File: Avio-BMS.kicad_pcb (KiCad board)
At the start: 2 copper layers, 80 x 80 mm, 102 parts, among them J1 MainBattery, J2 5077CR-16SMC2-BK-TR, J3 SubBattery, J4 Conn_01x03_Pin, J5 Conn_01x03_Pin, J6 +3.3V, J7 +6V, J8 +3.3V, J9 +6V, Q1 Si2333DDS-T1-GE3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

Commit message: update pcb
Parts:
- added C37: 0.1u, Capacitor_SMD:C_0603_1608Metric_Pad1.08x0.95mm_HandSolder, F.Cu at (157.2, 73.9)
- added C38: 1u, Capacitor_SMD:C_0603_1608Metric_Pad1.08x0.95mm_HandSolder, F.Cu at (160.4, 68.6)
- added C39: 43p, Capacitor_SMD:C_0603_1608Metric_Pad1.08x0.95mm_HandSolder, F.Cu at (165.7, 70.5)
- added C40: 1n, Capacitor_SMD:C_0603_1608Metric_Pad1.08x0.95mm_HandSolder, F.Cu at (167.3, 67.2)
- added R30: 28.7k, Resistor_SMD:R_0603_1608Metric_Pad0.98x0.95mm_HandSolder, F.Cu at (167.3, 70.5)
- C27: value C -> 8.2n
- R26: value R -> 115k
- moved C20 2.17 mm to (153.8, 77.7)
- moved C22 2.17 mm to (151.8, 77.7)
- moved C27 1.72 mm to (160.4, 79.4)
- moved R26 1.56 mm to (164.2, 68.6)
- moved C24 1.31 mm to (158.8, 77.4)
- moved D3 1.14 mm to (168.2, 119.0)
- moved R14 1.14 mm to (167.0, 117.7)
- moved R28 1.14 mm to (169.2, 70.8)
- moved R27 1.12 mm to (171.6, 71.7)
- moved R25 0.31 mm to (158.7, 72.0)
- moved C29 0.30 mm to (174.2, 74.4)
- moved C31 0.30 mm to (172.2, 74.4)
- moved C33 0.30 mm to (168.2, 74.4)
- moved C35 0.30 mm to (170.2, 74.4)
- moved C28 0.25 mm to (166.0, 74.4)
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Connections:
- net FB_{TPS61088} renamed /DCDC3.3V&7.4VOutput/FB_{TPS61088}
- U3 pad 16: (no net) -> GND
- U3 pad 17: (no net) -> GND
- U3 pad 18: (no net) -> GND
- U3 pad 19: (no net) -> GND
- U3 pad 20: (no net) -> GND
- U3 pad 21: (no net) -> GND
- U3 pad 22: (no net) -> GND
- U3 pad 23: (no net) -> GND
- U3 pad 24: (no net) -> GND
- U3 pad 25: (no net) -> GND
- U3 pad 26: (no net) -> GND
- U3 pad 27: (no net) -> GND
- U3 pad 28: (no net) -> GND
- U3 pad 29: (no net) -> GND
- U3 pad 30: (no net) -> GND
- U4 pad 1: unconnected-(U4-VCC_{TPS61088}-Pad1) -> /DCDC3.3V&7.4VOutput/EN_{TPS61088}
- U4 pad 13: unconnected-(U4-MODE-Pad13) -> GND
- U4 pad 18: unconnected-(U4-COMP-Pad18) -> /DCDC3.3V&7.4VOutput/COMP_{TPS61088}
- U4 pad 2: EN_{TPS61088} -> /DCDC3.3V&7.4VOutput/EN_{TPS61088}
- U4 pad 8: unconnected-(U4-BOOT-Pad8) -> Net-(U4-BOOT)
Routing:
- net +3.3V: track 71.3 -> 86.9 mm
- net +6V: track 100.0 -> 89.7 mm
- net VCC: track 91.0 -> 99.2 mm, vias 0 -> 2
- net /DCDC3.3V&7.4VOutput/COMP_{TPS61088}: track 0.00 -> 3.80 mm
- net NTC2: track 42.7 -> 39.2 mm
- net Net-(U4-BOOT): track 0.00 -> 3.38 mm
- net /DCDC3.3V&7.4VOutput/EN_{TPS61088}: track 0.00 -> 3.03 mm
- net NTC1: track 28.2 -> 25.7 mm
- net Net-(U4-SS): track 1.94 -> 3.61 mm
- net Net-(C40-Pad2): track 0.00 -> 1.53 mm
- net /DCDC3.3V&7.4VOutput/FB_{TPS61088}: track 6.20 -> 7.28 mm
- net GND: vias 10 -> 125
- added copper zone on F.Cu, net +6V
- added copper zone on B.Cu, net GND
- added copper zone on F.Cu, net GND
- added copper zone on F.Cu, net VCC

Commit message: update
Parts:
- moved D4 56.2 mm to (188.1, 104.5), turned to -90 degrees
- moved REF** 55.4 mm to (182.8, 111.2), turned to -45 degrees
- moved REF** 55.0 mm to (182.8, 60.3), turned to -45 degrees
- moved R23 54.3 mm to (186.5, 104.5), turned to 90 degrees
- moved D5 53.9 mm to (188.3, 100.5), turned to -90 degrees
- moved J3 52.5 mm to (189.3, 93.8), turned to 90 degrees
- moved D2 52.2 mm to (164.7, 50.5), turned to 0 degrees
- moved D3 51.9 mm to (186.6, 70.5), turned to 135 degrees
- moved R24 51.7 mm to (186.5, 100.6), turned to 90 degrees
- moved J1 51.3 mm to (189.3, 82.8), turned to 90 degrees
- moved TP1 50.1 mm to (175.0, 57.6), turned to -90 degrees
- moved R4 49.9 mm to (167.0, 53.1), turned to -90 degrees
- moved R14 49.5 mm to (185.4, 71.8), turned to 135 degrees
- moved REF** 47.2 mm to (131.9, 111.2), turned to -45 degrees
- moved J8 46.7 mm to (160.3, 117.8), turned to 0 degrees
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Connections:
- J5 pad 2: /Li-ionBatteryCharger,PowerPath/D1 -> /Li-ionBatteryCharger,PowerPath/D2
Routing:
- net /Li-ionBatteryCharger,PowerPath/D2: track 0.00 -> 16.3 mm, vias 0 -> 1
- net (no net): track 16.3 -> 0.00 mm, vias 1 -> 0
- net Net-(U3-EN): track 2.13 -> 17.3 mm, vias 0 -> 2
- net V1: track 94.6 -> 87.8 mm, vias 27 -> 33
- net VCC: track 99.2 -> 97.2 mm
- net Net-(Q3B-S2): track 35.1 -> 35.7 mm
- net GND: vias 125 -> 449

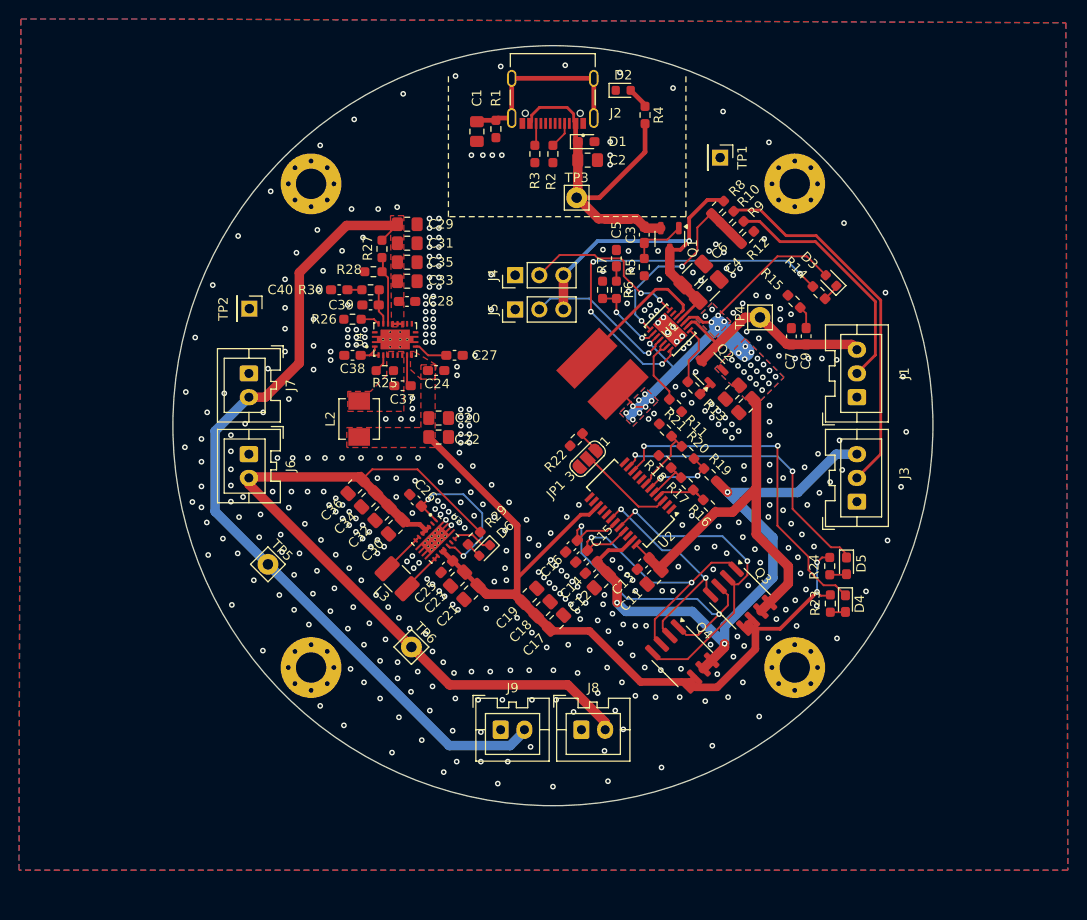
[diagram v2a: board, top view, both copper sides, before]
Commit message: remove autosave and lock files; update component values and footprints; add new drill and Gerber files; create BOM
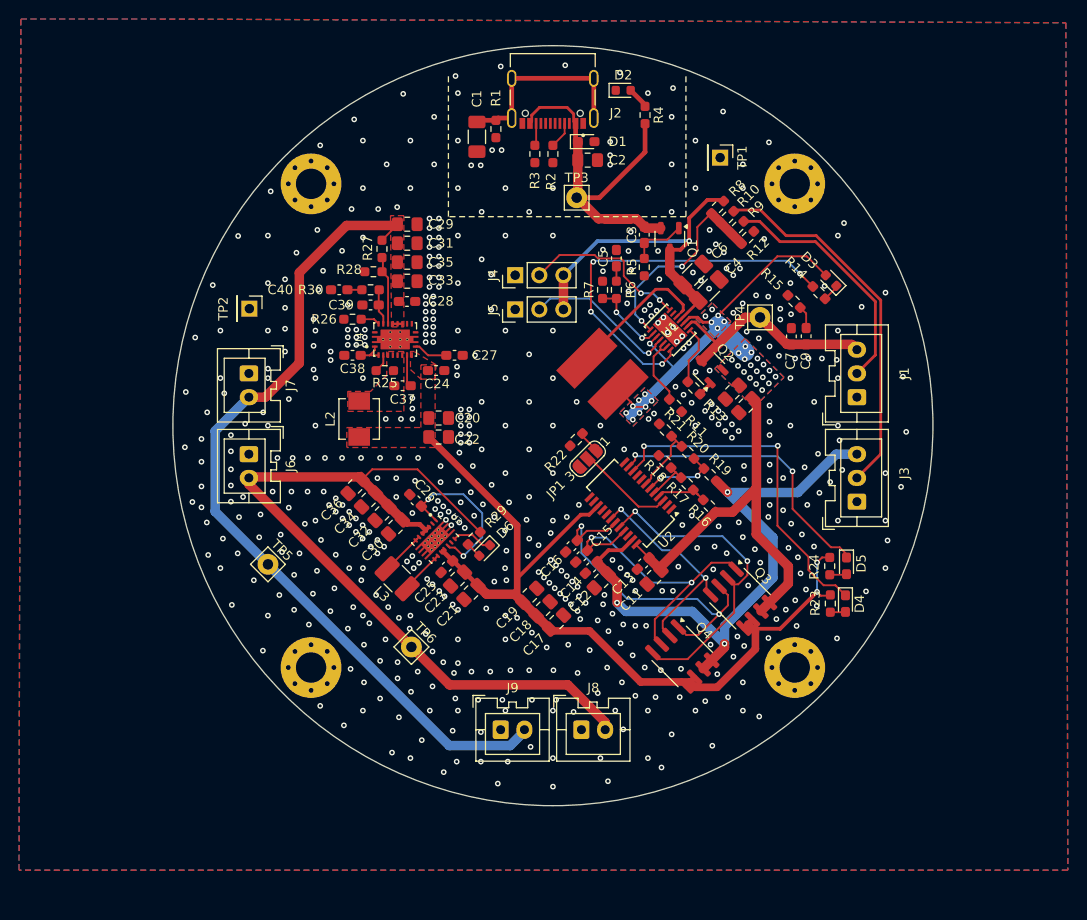
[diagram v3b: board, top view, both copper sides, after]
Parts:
- removed REF** (x4): MountingHole_3.2mm_M3_Pad_Via, MountingHole:MountingHole_3.2mm_M3_Pad_Via
- added H1: MountingHole_Pad, MountingHole:MountingHole_3.2mm_M3_Pad_Via, F.Cu at (182.8, 60.3)
- added H2: MountingHole_Pad, MountingHole:MountingHole_3.2mm_M3_Pad_Via, F.Cu at (182.8, 111.2)
- added H3: MountingHole_Pad, MountingHole:MountingHole_3.2mm_M3_Pad_Via, F.Cu at (131.9, 111.2)
- added H4: MountingHole_Pad, MountingHole:MountingHole_3.2mm_M3_Pad_Via, F.Cu at (131.9, 60.3)
- C1: value 10u -> 4700p; footprint Capacitor_SMD:C_0805_2012Metric_Pad1.18x1.45mm_HandSolder -> Capacitor_SMD:C_1206_3216Metric_Pad1.33x1.80mm_HandSolder
- moved C1 0.55 mm to (149.3, 55.4)
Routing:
- net GND: vias 449 -> 546
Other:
- board text added: "Avio-BMS"
